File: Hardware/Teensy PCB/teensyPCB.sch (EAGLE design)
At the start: 6 parts, among them U1 HC_05, U2 USD-SOCKETNEW

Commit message: Updated OLED module library and added modules to teensy PCB
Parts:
- added U$2, U$3: IIC128X64OLED, IIC OLED MODULE LIBRARY:IIC128X64OLED
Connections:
- new net SCL0: U$1.19/A5/T/SCL0, U$2.SCL
- new net SCL1: U$1.29/A18/SCL1, U$3.SCL
- new net SDA0: U$1.18/A4/T/SDA0, U$2.SDA
- new net SDA1: U$1.30/A19/SDA1, U$3.SDA
- net 3.3V: now also U$2.VCC, U$3.VCC
- net GND: now also U$2.GND, U$3.GND
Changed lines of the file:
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@@
 <?xml version="1.0" encoding="utf-8"?>
 <!DOCTYPE eagle SYSTEM "eagle.dtd">
-<eagle version="7.5.0">
+<eagle version="7.2.0">
 <drawing>
 <settings>
@@
 <setting verticaltext="up"/>
 </settings>
-<grid distance="0.1" unitdist="inch" unit="inch" style="lines" multiple="1" display="no" altdistance="0.01" altunitdist="inch" altunit="inch"/>
+<grid distance="0.1" unitdist="inch" unit="inch" style="lines" multiple="1" display="yes" altdistance="0.01" altunitdist="inch" altunit="inch"/>
 <layers>
 <layer number="1" name="Top" color="4" fill="1" visible="no" active="no"/>
@@
 <part name="GND4" library="SparkFun-Aesthetics" deviceset="GND" device=""/>
 <part name="SUPPLY4" library="SparkFun-Aesthetics" deviceset="3.3V" device=""/>
+<part name="U$2" library="IIC OLED MODULE LIBRARY" deviceset="IIC128X64OLED" device=""/>
+<part name="SUPPLY5" library="SparkFun-Aesthetics" deviceset="3.3V" device=""/>
+<part name="GND5" library="SparkFun-Aesthetics" deviceset="GND" device=""/>
+<part name="U$3" library="IIC OLED MODULE LIBRARY" deviceset="IIC128X64OLED" device=""/>
+<part name="SUPPLY6" library="SparkFun-Aesthetics" deviceset="3.3V" device=""/>
+<part name="GND6" library="SparkFun-Aesthetics" deviceset="GND" device=""/>
 </parts>
 <sheets>
@@
 <instance part="GND4" gate="1" x="-60.96" y="-5.08" rot="R270"/>
 <instance part="SUPPLY4" gate="G$1" x="-58.42" y="0" rot="R90"/>
+<instance part="U$2" gate="G$1" x="-27.94" y="66.04"/>
+<instance part="SUPPLY5" gate="G$1" x="-2.54" y="73.66" rot="R270"/>
+<instance part="GND5" gate="1" x="0" y="66.04" rot="R90"/>
+<instance part="U$3" gate="G$1" x="17.78" y="66.04"/>
+<instance part="SUPPLY6" gate="G$1" x="43.18" y="73.66" rot="R270"/>
+<instance part="GND6" gate="1" x="45.72" y="66.04" rot="R90"/>
 </instances>
 <busses>
@@
 <wire x1="-50.8" y1="-5.08" x2="-58.42" y2="-5.08" width="0.1524" layer="91"/>
 </segment>
+<segment>
+<pinref part="U$2" gate="G$1" pin="GND"/>
+<wire x1="-2.54" y1="66.04" x2="-6.35" y2="66.04" width="0.1524" layer="91"/>
+<pinref part="GND5" gate="1" pin="GND"/>
+</segment>
+<segment>
+<pinref part="U$3" gate="G$1" pin="GND"/>
+<wire x1="43.18" y1="66.04" x2="39.37" y2="66.04" width="0.1524" layer="91"/>
+<pinref part="GND6" gate="1" pin="GND"/>
+</segment>
 </net>
 <net name="3.3V" class="0">
@@
 <wire x1="-50.8" y1="0" x2="-58.42" y2="0" width="0.1524" layer="91"/>
 </segment>
+<segment>
+<pinref part="U$2" gate="G$1" pin="VCC"/>
+<wire x1="-2.54" y1="73.66" x2="-6.35" y2="73.66" width="0.1524" layer="91"/>
+<pinref part="SUPPLY5" gate="G$1" pin="3.3V"/>
+</segment>
+<segment>
+<pinref part="U$3" gate="G$1" pin="VCC"/>
+<wire x1="43.18" y1="73.66" x2="39.37" y2="73.66" width="0.1524" layer="91"/>
+<pinref part="SUPPLY6" gate="G$1" pin="3.3V"/>
+</segment>
 </net>
 <net name="5V" class="0">
@@
 </segment>
 </net>
+<net name="SDA0" class="0">
+<segment>
+<pinref part="U$1" gate="G$1" pin="18/A4/T/SDA0"/>
+<wire x1="-17.78" y1="-2.54" x2="-20.32" y2="-2.54" width="0.1524" layer="91"/>
+<label x="-20.32" y="-2.54" size="1.778" layer="95"/>
+</segment>
+<segment>
+<pinref part="U$2" gate="G$1" pin="SDA"/>
+<wire x1="-2.54" y1="68.58" x2="-6.35" y2="68.58" width="0.1524" layer="91"/>
+<label x="-5.08" y="68.58" size="1.778" layer="95"/>
+</segment>
+</net>
+<net name="SCL0" class="0">
+<segment>
+<pinref part="U$1" gate="G$1" pin="19/A5/T/SCL0"/>
+<wire x1="-17.78" y1="-5.08" x2="-20.32" y2="-5.08" width="0.1524" layer="91"/>
+<label x="-20.32" y="-5.08" size="1.778" layer="95"/>
+</segment>
+<segment>
+<pinref part="U$2" gate="G$1" pin="SCL"/>
+<wire x1="-2.54" y1="71.12" x2="-6.35" y2="71.12" width="0.1524" layer="91"/>
+<label x="-5.08" y="71.12" size="1.778" layer="95"/>
+</segment>
+</net>
+<net name="SDA1" class="0">
+<segment>
+<pinref part="U$1" gate="G$1" pin="30/A19/SDA1"/>
+<wire x1="27.94" y1="-5.08" x2="30.48" y2="-5.08" width="0.1524" layer="91"/>
+<label x="27.94" y="-5.08" size="1.778" layer="95"/>
+</segment>
+<segment>
+<pinref part="U$3" gate="G$1" pin="SDA"/>
+<wire x1="43.18" y1="68.58" x2="39.37" y2="68.58" width="0.1524" layer="91"/>
+<label x="40.64" y="68.58" size="1.778" layer="95"/>
+</segment>
+</net>
+<net name="SCL1" class="0">
+<segment>
+<pinref part="U$1" gate="G$1" pin="29/A18/SCL1"/>
+<wire x1="27.94" y1="-7.62" x2="30.48" y2="-7.62" width="0.1524" layer="91"/>
+<label x="27.94" y="-7.62" size="1.778" layer="95"/>
+</segment>
+<segment>
+<pinref part="U$3" gate="G$1" pin="SCL"/>
+<wire x1="43.18" y1="71.12" x2="39.37" y2="71.12" width="0.1524" layer="91"/>
+<label x="40.64" y="71.12" size="1.778" layer="95"/>
+</segment>
+</net>

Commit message: Added audio amp to pcb
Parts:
- added U$4: AUDIOAMP, CLASS D AUDIO AMP:AUDIOAMP
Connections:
- net 5V: now also U$4.+5V
- net GND: now also U$4.GND0, U$4.GND1, U$4.GND2
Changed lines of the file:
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@@
 <part name="SUPPLY6" library="SparkFun-Aesthetics" deviceset="3.3V" device=""/>
 <part name="GND6" library="SparkFun-Aesthetics" deviceset="GND" device=""/>
+<part name="SUPPLY7" library="SparkFun-Aesthetics" deviceset="5V" device=""/>
+<part name="GND7" library="SparkFun-Aesthetics" deviceset="GND" device=""/>
+<part name="GND8" library="SparkFun-Aesthetics" deviceset="GND" device=""/>
+<part name="GND9" library="SparkFun-Aesthetics" deviceset="GND" device=""/>
+<part name="U$4" library="CLASS D AUDIO AMP" deviceset="AUDIOAMP" device=""/>
 </parts>
 <sheets>
@@
 <instance part="SUPPLY6" gate="G$1" x="43.18" y="73.66" rot="R270"/>
 <instance part="GND6" gate="1" x="45.72" y="66.04" rot="R90"/>
+<instance part="SUPPLY7" gate="G$1" x="53.34" y="-10.16" rot="R90"/>
+<instance part="GND7" gate="1" x="55.88" y="-15.24" rot="R270"/>
+<instance part="GND8" gate="1" x="55.88" y="-7.62" rot="R270"/>
+<instance part="GND9" gate="1" x="55.88" y="-20.32" rot="R270"/>
+<instance part="U$4" gate="G$1" x="73.66" y="-10.16"/>
 </instances>
 <busses>
@@
 <wire x1="43.18" y1="66.04" x2="39.37" y2="66.04" width="0.1524" layer="91"/>
 <pinref part="GND6" gate="1" pin="GND"/>
+</segment>
+<segment>
+<pinref part="GND8" gate="1" pin="GND"/>
+<pinref part="U$4" gate="G$1" pin="GND0"/>
+<wire x1="58.42" y1="-7.62" x2="60.96" y2="-7.62" width="0.1524" layer="91"/>
+</segment>
+<segment>
+<pinref part="GND7" gate="1" pin="GND"/>
+<pinref part="U$4" gate="G$1" pin="GND1"/>
+<wire x1="58.42" y1="-15.24" x2="60.96" y2="-15.24" width="0.1524" layer="91"/>
+</segment>
+<segment>
+<pinref part="GND9" gate="1" pin="GND"/>
+<pinref part="U$4" gate="G$1" pin="GND2"/>
+<wire x1="58.42" y1="-20.32" x2="60.96" y2="-20.32" width="0.1524" layer="91"/>
 </segment>
 </net>
@@
 <wire x1="-48.26" y1="33.02" x2="-55.88" y2="33.02" width="0.1524" layer="91"/>
 </segment>
+<segment>
+<pinref part="SUPPLY7" gate="G$1" pin="5V"/>
+<pinref part="U$4" gate="G$1" pin="+5V"/>
+<wire x1="53.34" y1="-10.16" x2="60.96" y2="-10.16" width="0.1524" layer="91"/>
+</segment>
 </net>

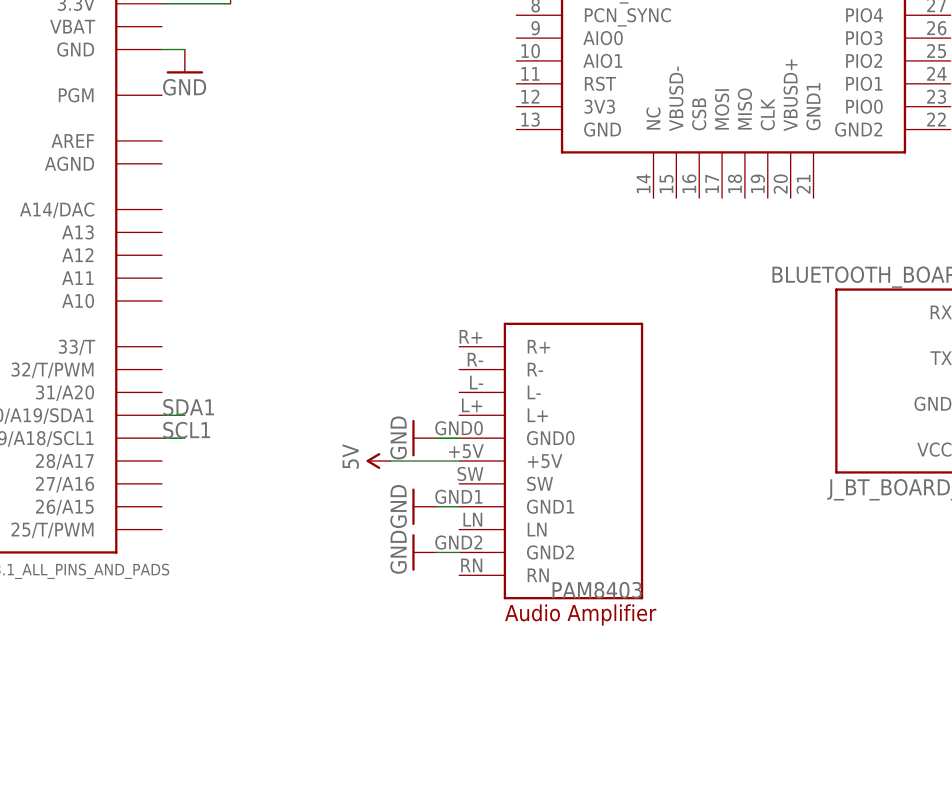
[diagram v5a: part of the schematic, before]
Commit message: First attempt at wiring the audio (could be totally wrong)
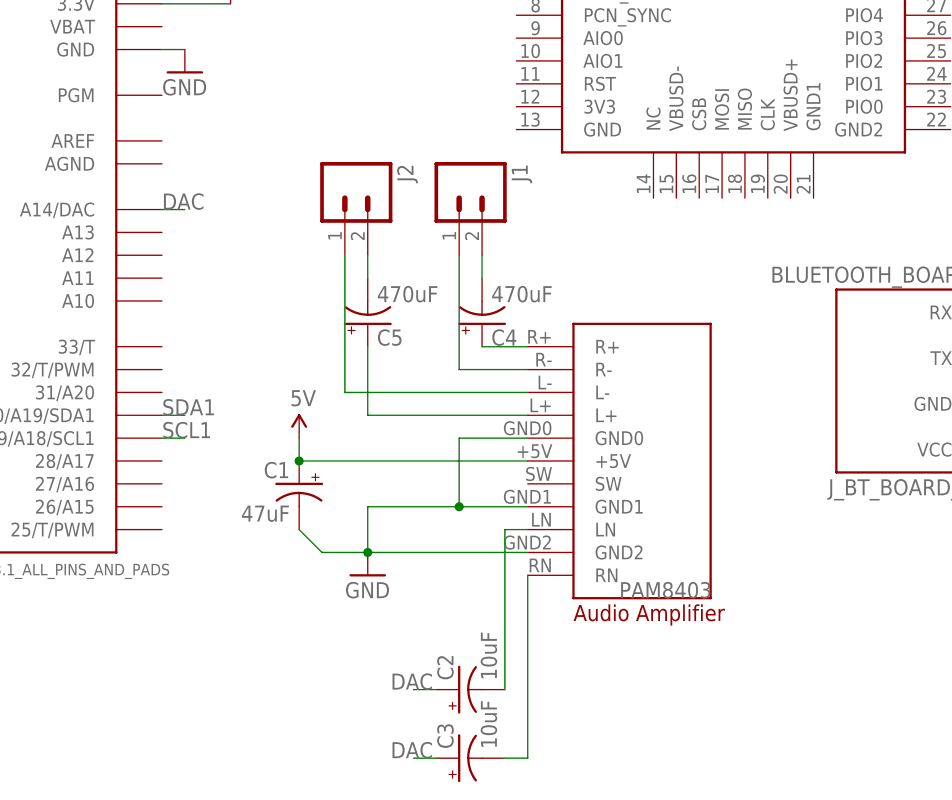
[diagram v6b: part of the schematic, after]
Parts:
- added C1: 47uF, SparkFun-Capacitors:CAP_POL3528
- added C2, C3: 10uF, SparkFun-Capacitors:CAP_POL3528
- added C4, C5: 470uF, SparkFun-Capacitors:CAP_POL3528
- added J1, J2: (no value), SparkFun-Connectors:M02PTH
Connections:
- new net DAC: C2.+, C3.+, U$1.A14/DAC
- new net N$1: C2.-, U$4.LN
- new net N$2: C3.-, U$4.RN
- new net N$3: C4.-, J1.2
- new net N$4: C5.-, J2.2
- new net N$5: C4.+, U$4.R+
- new net N$6: J1.1, U$4.R-
- new net N$7: J2.1, U$4.L-
- new net N$8: C5.+, U$4.L+
- net 5V: now also C1.+
- net GND: now also C1.-
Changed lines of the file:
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@@
 <layer number="56" name="wert" color="7" fill="1" visible="no" active="no"/>
 <layer number="57" name="tCAD" color="7" fill="1" visible="no" active="no"/>
+<layer number="59" name="tCarbon" color="7" fill="1" visible="no" active="no"/>
+<layer number="60" name="bCarbon" color="7" fill="1" visible="no" active="no"/>
 <layer number="90" name="Modules" color="5" fill="1" visible="yes" active="yes"/>
 <layer number="91" name="Nets" color="2" fill="1" visible="yes" active="yes"/>
@@
 <layer number="112" name="tSilk" color="7" fill="1" visible="yes" active="yes"/>
 <layer number="113" name="IDFDebug" color="4" fill="1" visible="yes" active="yes"/>
+<layer number="114" name="Badge_Outline" color="7" fill="1" visible="yes" active="yes"/>
+<layer number="115" name="ReferenceISLANDS" color="7" fill="1" visible="yes" active="yes"/>
 <layer number="116" name="Patch_BOT" color="9" fill="4" visible="yes" active="yes"/>
+<layer number="118" name="Rect_Pads" color="7" fill="1" visible="yes" active="yes"/>
 <layer number="121" name="_tsilk" color="7" fill="1" visible="yes" active="yes"/>
 <layer number="122" name="_bsilk" color="7" fill="1" visible="yes" active="yes"/>
@@
 <layer number="127" name="_tValues" color="7" fill="1" visible="yes" active="yes"/>
 <layer number="128" name="_bValues" color="7" fill="1" visible="yes" active="yes"/>
+<layer number="129" name="Mask" color="7" fill="1" visible="yes" active="yes"/>
 <layer number="131" name="tAdjust" color="7" fill="1" visible="yes" active="yes"/>
 <layer number="132" name="bAdjust" color="7" fill="1" visible="yes" active="yes"/>
@@
 <layer number="223" name="223bmp" color="24" fill="1" visible="no" active="no"/>
 <layer number="224" name="224bmp" color="25" fill="1" visible="no" active="no"/>
+<layer number="225" name="225bmp" color="7" fill="1" visible="yes" active="yes"/>
+<layer number="226" name="226bmp" color="7" fill="1" visible="yes" active="yes"/>
+<layer number="227" name="227bmp" color="7" fill="1" visible="yes" active="yes"/>
+<layer number="228" name="228bmp" color="7" fill="1" visible="yes" active="yes"/>
+<layer number="229" name="229bmp" color="7" fill="1" visible="yes" active="yes"/>
+<layer number="230" name="230bmp" color="7" fill="1" visible="yes" active="yes"/>
+<layer number="231" name="231bmp" color="7" fill="1" visible="yes" active="yes"/>
 <layer number="248" name="Housing" color="7" fill="1" visible="yes" active="yes"/>
 <layer number="249" name="Edge" color="7" fill="1" visible="yes" active="yes"/>
@@
 <layer number="251" name="SMDround" color="12" fill="11" visible="no" active="no"/>
 <layer number="254" name="cooling" color="7" fill="1" visible="yes" active="yes"/>
+<layer number="255" name="routoute" color="7" fill="1" visible="yes" active="yes"/>
 </layers>
 <schematic xreflabel="%F%N/%S.%C%R" xrefpart="/%S.%C%R">
@@
 <part name="GND6" library="SparkFun-Aesthetics" deviceset="GND" device=""/>
 <part name="SUPPLY7" library="SparkFun-Aesthetics" deviceset="5V" device=""/>
-<part name="GND7" library="SparkFun-Aesthetics" deviceset="GND" device=""/>
-<part name="GND8" library="SparkFun-Aesthetics" deviceset="GND" device=""/>
 <part name="GND9" library="SparkFun-Aesthetics" deviceset="GND" device=""/>
 <part name="U$4" library="CLASS D AUDIO AMP" deviceset="AUDIOAMP" device=""/>
+<part name="C1" library="SparkFun-Capacitors" deviceset="CAP_POL" device="3528" value="47uF"/>
+<part name="C2" library="SparkFun-Capacitors" deviceset="CAP_POL" device="3528" value="10uF"/>
+<part name="C3" library="SparkFun-Capacitors" deviceset="CAP_POL" device="3528" value="10uF"/>
+<part name="J1" library="SparkFun-Connectors" deviceset="M02" device="PTH"/>
+<part name="J2" library="SparkFun-Connectors" deviceset="M02" device="PTH"/>
+<part name="C4" library="SparkFun-Capacitors" deviceset="CAP_POL" device="3528" value="470uF"/>
+<part name="C5" library="SparkFun-Capacitors" deviceset="CAP_POL" device="3528" value="470uF"/>
 </parts>
 <sheets>
@@
 <instance part="SUPPLY6" gate="G$1" x="43.18" y="73.66" rot="R270"/>
 <instance part="GND6" gate="1" x="45.72" y="66.04" rot="R90"/>
-<instance part="SUPPLY7" gate="G$1" x="53.34" y="-10.16" rot="R90"/>
-<instance part="GND7" gate="1" x="55.88" y="-15.24" rot="R270"/>
-<instance part="GND8" gate="1" x="55.88" y="-7.62" rot="R270"/>
-<instance part="GND9" gate="1" x="55.88" y="-20.32" rot="R270"/>
-<instance part="U$4" gate="G$1" x="73.66" y="-10.16"/>
+<instance part="SUPPLY7" gate="G$1" x="43.18" y="-7.62"/>
+<instance part="GND9" gate="1" x="50.8" y="-22.86"/>
+<instance part="U$4" gate="G$1" x="81.28" y="-10.16"/>
+<instance part="C1" gate="G$1" x="43.18" y="-12.7" rot="MR0"/>
+<instance part="C2" gate="G$1" x="60.96" y="-35.56" rot="R90"/>
+<instance part="C3" gate="G$1" x="60.96" y="-43.18" rot="R90"/>
+<instance part="J1" gate="G$1" x="60.96" y="20.32" rot="R270"/>
+<instance part="J2" gate="G$1" x="48.26" y="20.32" rot="R270"/>
+<instance part="C4" gate="G$1" x="63.5" y="5.08" rot="MR180"/>
+<instance part="C5" gate="G$1" x="50.8" y="5.08" rot="MR180"/>
 </instances>
 <busses>
@@
 </segment>
 <segment>
-<pinref part="GND8" gate="1" pin="GND"/>
-<pinref part="U$4" gate="G$1" pin="GND0"/>
-<wire x1="58.42" y1="-7.62" x2="60.96" y2="-7.62" width="0.1524" layer="91"/>
-</segment>
-<segment>
-<pinref part="GND7" gate="1" pin="GND"/>
-<pinref part="U$4" gate="G$1" pin="GND1"/>
-<wire x1="58.42" y1="-15.24" x2="60.96" y2="-15.24" width="0.1524" layer="91"/>
-</segment>
-<segment>
 <pinref part="GND9" gate="1" pin="GND"/>
 <pinref part="U$4" gate="G$1" pin="GND2"/>
-<wire x1="58.42" y1="-20.32" x2="60.96" y2="-20.32" width="0.1524" layer="91"/>
+<wire x1="50.8" y1="-20.32" x2="68.58" y2="-20.32" width="0.1524" layer="91"/>
+<pinref part="U$4" gate="G$1" pin="GND1"/>
+<wire x1="50.8" y1="-15.24" x2="60.96" y2="-15.24" width="0.1524" layer="91"/>
+<wire x1="60.96" y1="-15.24" x2="68.58" y2="-15.24" width="0.1524" layer="91"/>
+<wire x1="50.8" y1="-15.24" x2="50.8" y2="-20.32" width="0.1524" layer="91"/>
+<junction x="50.8" y="-20.32"/>
+<pinref part="C1" gate="G$1" pin="-"/>
+<wire x1="43.18" y1="-17.78" x2="45.72" y2="-20.32" width="0.1524" layer="91"/>
+<wire x1="45.72" y1="-20.32" x2="50.8" y2="-20.32" width="0.1524" layer="91"/>
+<pinref part="U$4" gate="G$1" pin="GND0"/>
+<wire x1="68.58" y1="-7.62" x2="60.96" y2="-7.62" width="0.1524" layer="91"/>
+<wire x1="60.96" y1="-7.62" x2="60.96" y2="-15.24" width="0.1524" layer="91"/>
+<junction x="60.96" y="-15.24"/>
 </segment>
 </net>
@@
 <pinref part="SUPPLY7" gate="G$1" pin="5V"/>
 <pinref part="U$4" gate="G$1" pin="+5V"/>
-<wire x1="53.34" y1="-10.16" x2="60.96" y2="-10.16" width="0.1524" layer="91"/>
+<wire x1="43.18" y1="-10.16" x2="68.58" y2="-10.16" width="0.1524" layer="91"/>
+<pinref part="C1" gate="G$1" pin="+"/>
+<junction x="43.18" y="-10.16"/>
+<wire x1="43.18" y1="-10.16" x2="43.18" y2="-7.62" width="0.1524" layer="91"/>
 </segment>
 </net>
@@
 </segment>
 </net>
+<net name="N$1" class="0">
+<segment>
+<pinref part="U$4" gate="G$1" pin="LN"/>
+<pinref part="C2" gate="G$1" pin="-"/>
+<wire x1="68.58" y1="-17.78" x2="66.04" y2="-17.78" width="0.1524" layer="91"/>
+<wire x1="66.04" y1="-17.78" x2="66.04" y2="-35.56" width="0.1524" layer="91"/>
+</segment>
+</net>
+<net name="N$2" class="0">
+<segment>
+<pinref part="U$4" gate="G$1" pin="RN"/>
+<wire x1="68.58" y1="-22.86" x2="68.58" y2="-43.18" width="0.1524" layer="91"/>
+<pinref part="C3" gate="G$1" pin="-"/>
+<wire x1="68.58" y1="-43.18" x2="66.04" y2="-43.18" width="0.1524" layer="91"/>
+</segment>
+</net>
+<net name="DAC" class="0">
+<segment>
+<pinref part="U$1" gate="G$1" pin="A14/DAC"/>
+<wire x1="27.94" y1="17.78" x2="30.48" y2="17.78" width="0.1524" layer="91"/>
+<label x="27.94" y="17.78" size="1.778" layer="95"/>
+</segment>
+<segment>
+<pinref part="C2" gate="G$1" pin="+"/>
+<wire x1="58.42" y1="-35.56" x2="55.88" y2="-35.56" width="0.1524" layer="91"/>
+<label x="53.34" y="-35.56" size="1.778" layer="95"/>
+</segment>
+<segment>
+<pinref part="C3" gate="G$1" pin="+"/>
+<wire x1="58.42" y1="-43.18" x2="55.88" y2="-43.18" width="0.1524" layer="91"/>
+<label x="53.34" y="-43.18" size="1.778" layer="95"/>
+</segment>
+</net>
+<net name="N$3" class="0">
+<segment>
+<pinref part="J1" gate="G$1" pin="2"/>
+<pinref part="C4" gate="G$1" pin="-"/>
+<wire x1="63.5" y1="12.7" x2="63.5" y2="10.16" width="0.1524" layer="91"/>
+</segment>
+</net>
+<net name="N$4" class="0">
+<segment>
+<pinref part="J2" gate="G$1" pin="2"/>
+<pinref part="C5" gate="G$1" pin="-"/>
+<wire x1="50.8" y1="10.16" x2="50.8" y2="12.7" width="0.1524" layer="91"/>
+</segment>
+</net>
+<net name="N$5" class="0">
+<segment>
+<pinref part="C4" gate="G$1" pin="+"/>
+<pinref part="U$4" gate="G$1" pin="R+"/>
+<wire x1="63.5" y1="2.54" x2="68.58" y2="2.54" width="0.1524" layer="91"/>
+</segment>
+</net>
+<net name="N$6" class="0">
+<segment>
+<pinref part="J1" gate="G$1" pin="1"/>
+<wire x1="60.96" y1="12.7" x2="60.96" y2="0" width="0.1524" layer="91"/>
+<pinref part="U$4" gate="G$1" pin="R-"/>
+<wire x1="60.96" y1="0" x2="68.58" y2="0" width="0.1524" layer="91"/>
+</segment>
+</net>
+<net name="N$7" class="0">
+<segment>
+<pinref part="U$4" gate="G$1" pin="L-"/>
+<pinref part="J2" gate="G$1" pin="1"/>
+<wire x1="68.58" y1="-2.54" x2="48.26" y2="-2.54" width="0.1524" layer="91"/>
+<wire x1="48.26" y1="-2.54" x2="48.26" y2="12.7" width="0.1524" layer="91"/>
+</segment>
+</net>
+<net name="N$8" class="0">
+<segment>
+<pinref part="C5" gate="G$1" pin="+"/>
+<wire x1="50.8" y1="2.54" x2="50.8" y2="-5.08" width="0.1524" layer="91"/>
+<pinref part="U$4" gate="G$1" pin="L+"/>
+<wire x1="50.8" y1="-5.08" x2="68.58" y2="-5.08" width="0.1524" layer="91"/>
+</segment>
+</net>
